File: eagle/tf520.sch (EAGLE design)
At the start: 23 parts, among them IC1 MC68020, IC3 XC9536_44VQ, U1 LM1117, X1 MC68000

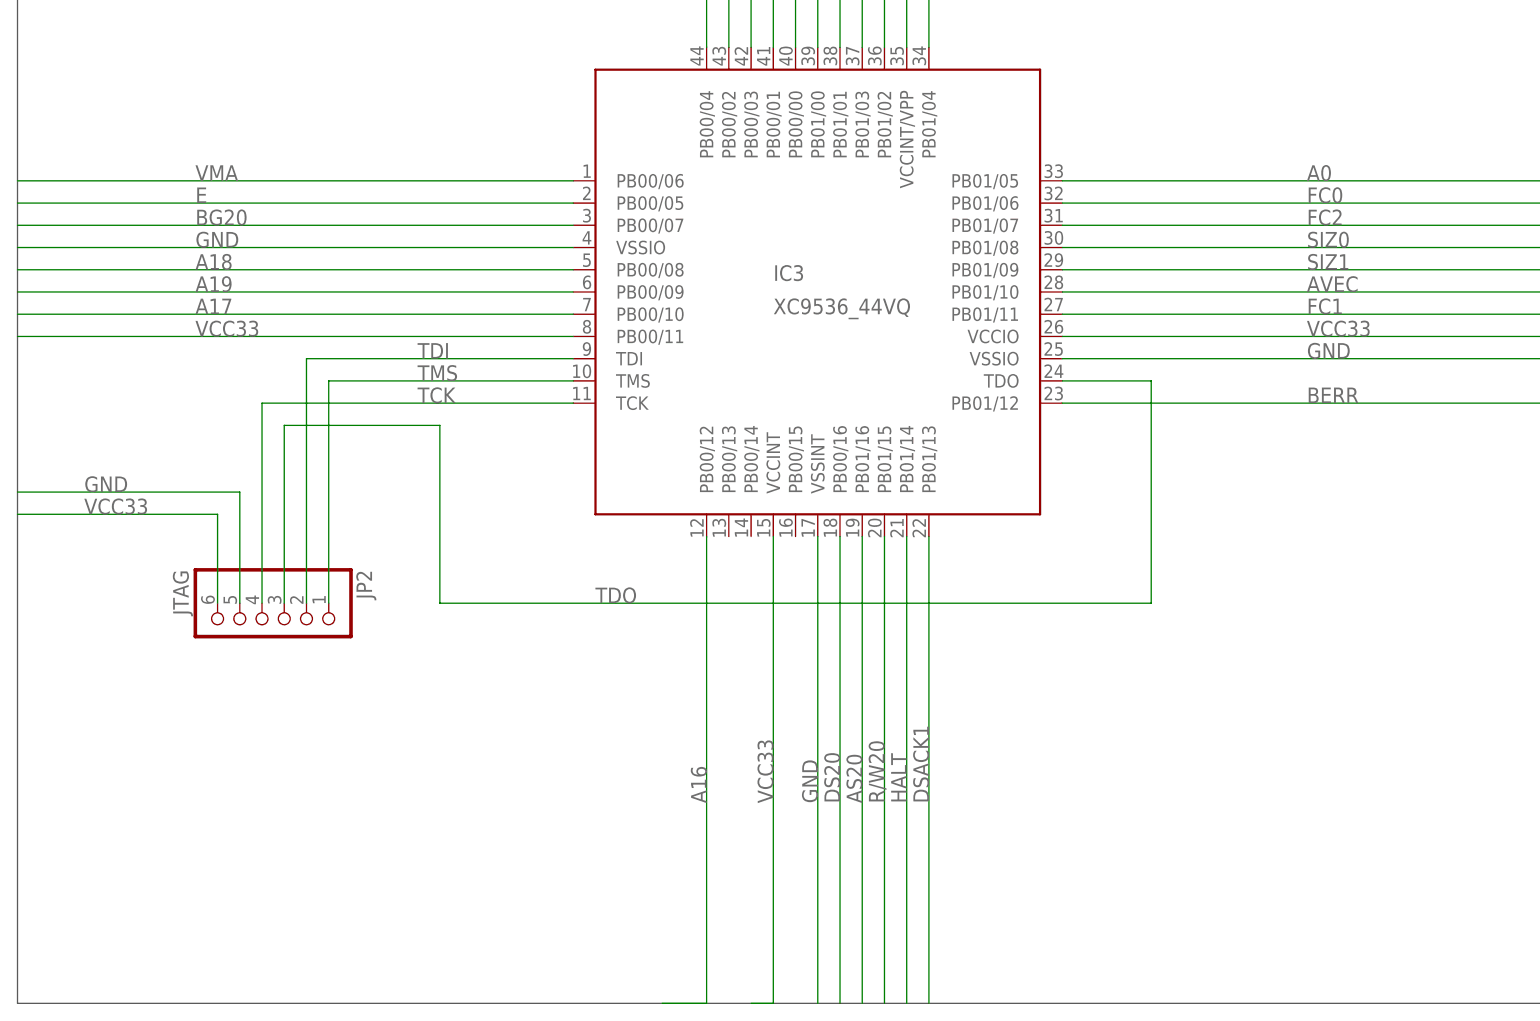
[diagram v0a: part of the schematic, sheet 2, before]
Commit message: Adding the Atari ST fixes Reorganizing the repos. Added jed files for rev 2 and rev 3 Published the REV 3 sources and ucf
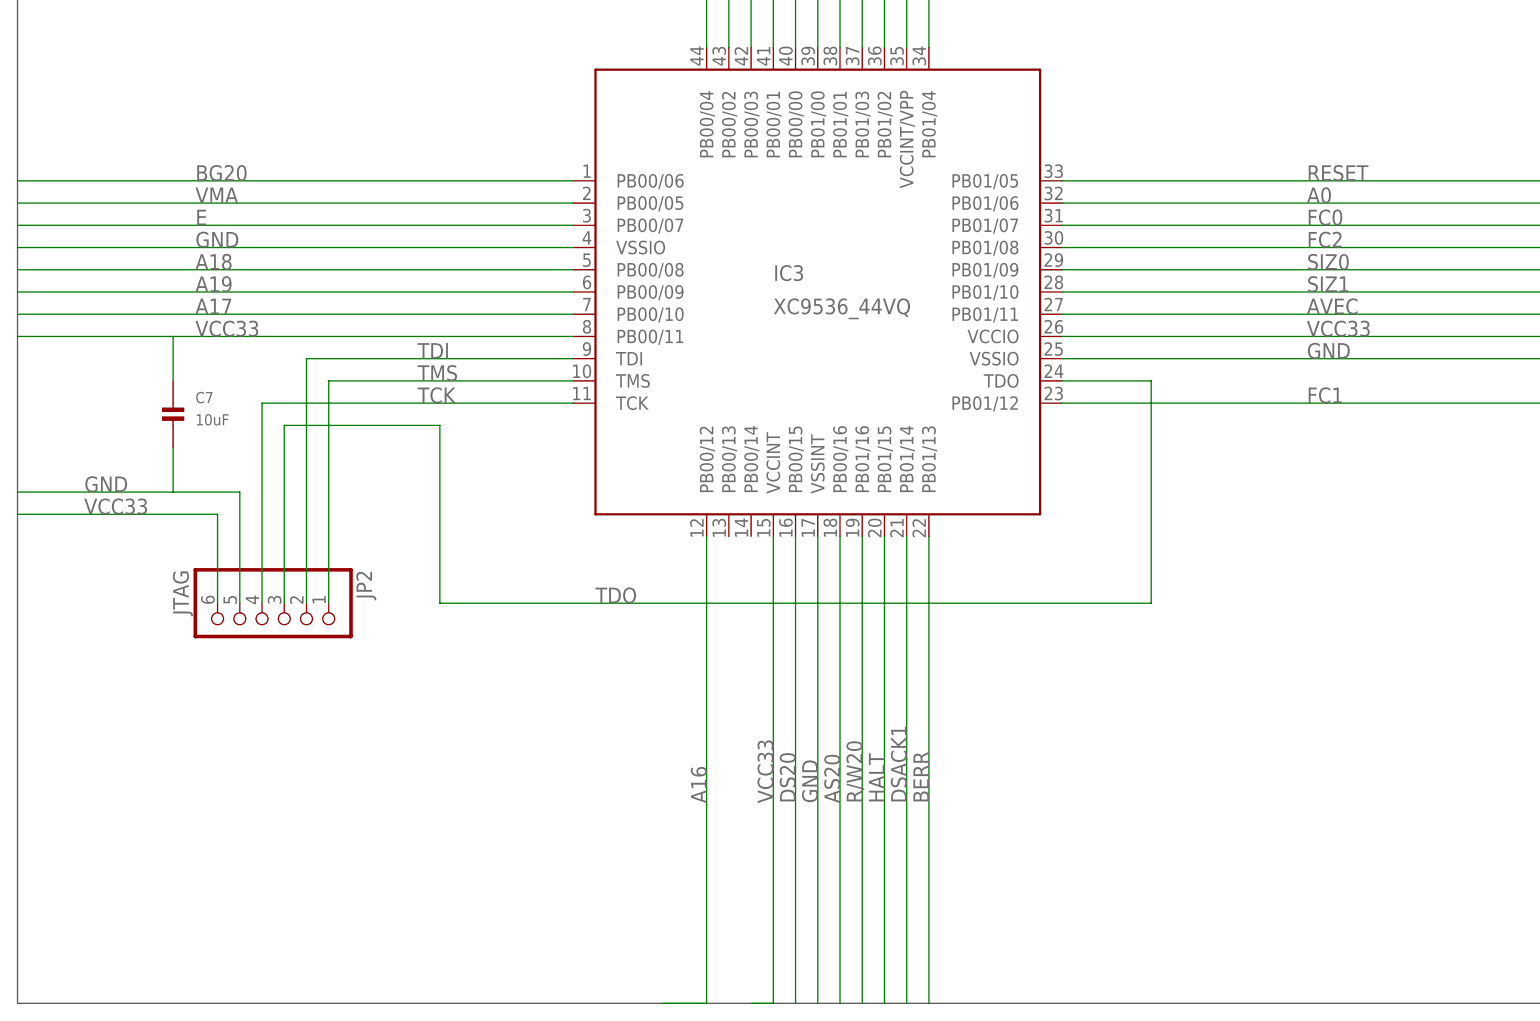
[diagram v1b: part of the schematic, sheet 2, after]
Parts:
- added C7: 10uF, microbuilder:CAP_CERAMIC1206
- added IC2: 74LVC1G17DBV, 74xx-little-de:74LVC1G17DBV
- JP4: device jumper:JP1E -> SparkFun-Retired:JUMPER-2PTH
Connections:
- new net CLK7M_RAW: IC2G$1.I, X1G$1.CLK
- net A0: now also IC3.PB01/06; no longer IC3.PB01/05
- net AS20: now also IC3.PB00/16; no longer IC3.PB01/16
- net AVEC: now also IC3.PB01/11; no longer IC3.PB01/10
- net BERR: now also IC3.PB01/13; no longer IC3.PB01/12
- net BG20: now also IC3.PB00/06; no longer IC3.PB00/07
- net CLK7M: now also IC2G$1.O; no longer X1G$1.CLK
- net DS20: now also IC3.PB00/15; no longer IC3.PB00/16
- net DSACK1: now also IC3.PB01/14; no longer IC3.PB01/13
- net E: now also IC3.PB00/07; no longer IC3.PB00/05
- net FC0: now also IC3.PB01/07; no longer IC3.PB01/06
- net FC1: now also IC3.PB01/12; no longer IC3.PB01/11
- net FC2: now also IC3.PB01/08; no longer IC3.PB01/07
- net GND: now also C7.P$2
- net HALT: now also IC3.PB01/15; no longer IC3.PB01/14
- net R/W20: now also IC3.PB01/16; no longer IC3.PB01/15
- net RESET: now also IC3.PB01/05
- net SIZ0: now also IC3.PB01/09; no longer IC3.PB01/08
- net SIZ1: now also IC3.PB01/10; no longer IC3.PB01/09
- net VCC33: now also C7.P$1
- net VMA: now also IC3.PB00/05; no longer IC3.PB00/06
